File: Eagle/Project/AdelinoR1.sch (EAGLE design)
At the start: 63 parts, among them J1 DC-044-A, J2 YELLOW-8P-2.54, J3 YELLOW-6P-2.54, J4 YELLOW-8P-2.54, J5 YELLOW-8P-2.54, J6 4P-2.0, J7 YELLOW-2X3P-2.54, J8 4P-2.0, Q1 NCE3407A, Q2 CJ2305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

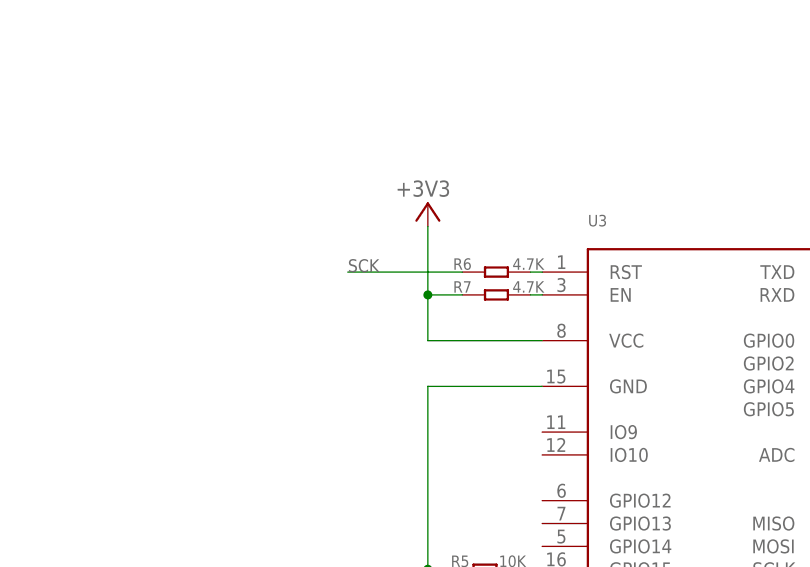
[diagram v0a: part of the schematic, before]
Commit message: Now SCK drives CHIP_EN instead of RST; RST pulled high using 4K7.
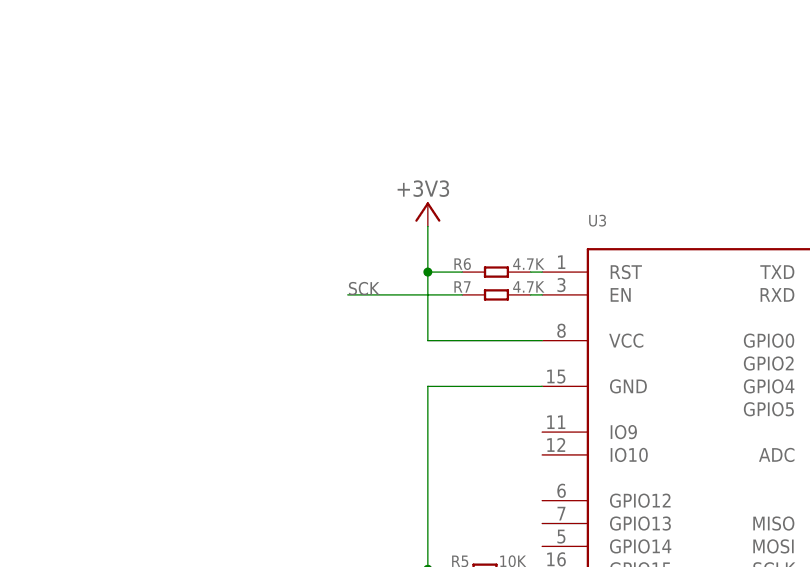
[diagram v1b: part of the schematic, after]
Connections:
- net +3V3: now also R6.1; no longer R7.1
- net SCK: now also R7.1; no longer R6.1
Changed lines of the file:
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@@
 <setting verticaltext="up"/>
 </settings>
-<grid distance="0.1" unitdist="inch" unit="inch" style="lines" multiple="1" display="no" altdistance="0.01" altunitdist="inch" altunit="inch"/>
+<grid distance="0.05" unitdist="inch" unit="inch" style="lines" multiple="1" display="no" altdistance="0.01" altunitdist="inch" altunit="inch"/>
 <layers>
 <layer number="1" name="Top" color="4" fill="1" visible="no" active="no"/>
@@
 <pinref part="+3V32" gate="G$1" pin="+3V3"/>
 <wire x1="93.98" y1="-78.74" x2="81.28" y2="-78.74" width="0.1524" layer="91"/>
-<wire x1="81.28" y1="-78.74" x2="81.28" y2="-73.66" width="0.1524" layer="91"/>
-<wire x1="81.28" y1="-73.66" x2="81.28" y2="-66.04" width="0.1524" layer="91"/>
-<wire x1="85.09" y1="-73.66" x2="81.28" y2="-73.66" width="0.1524" layer="91"/>
-<junction x="81.28" y="-73.66"/>
-<pinref part="R7" gate="G$1" pin="1"/>
+<wire x1="81.28" y1="-78.74" x2="81.28" y2="-71.12" width="0.1524" layer="91"/>
+<pinref part="R6" gate="G$1" pin="1"/>
+<wire x1="81.28" y1="-71.12" x2="81.28" y2="-66.04" width="0.1524" layer="91"/>
+<wire x1="85.09" y1="-71.12" x2="81.28" y2="-71.12" width="0.1524" layer="91"/>
+<junction x="81.28" y="-71.12"/>
 </segment>
 <segment>
@@
 </segment>
 <segment>
-<pinref part="R6" gate="G$1" pin="1"/>
-<wire x1="85.09" y1="-71.12" x2="72.39" y2="-71.12" width="0.1524" layer="91"/>
-<label x="72.39" y="-71.12" size="1.4224" layer="95"/>
-</segment>
-</net>
+<pinref part="R7" gate="G$1" pin="1"/>
+<wire x1="85.09" y1="-73.66" x2="72.39" y2="-73.66" width="0.1524" layer="91"/>
+<label x="72.39" y="-73.66" size="1.4224" layer="95"/>
+</segment>
+</net>

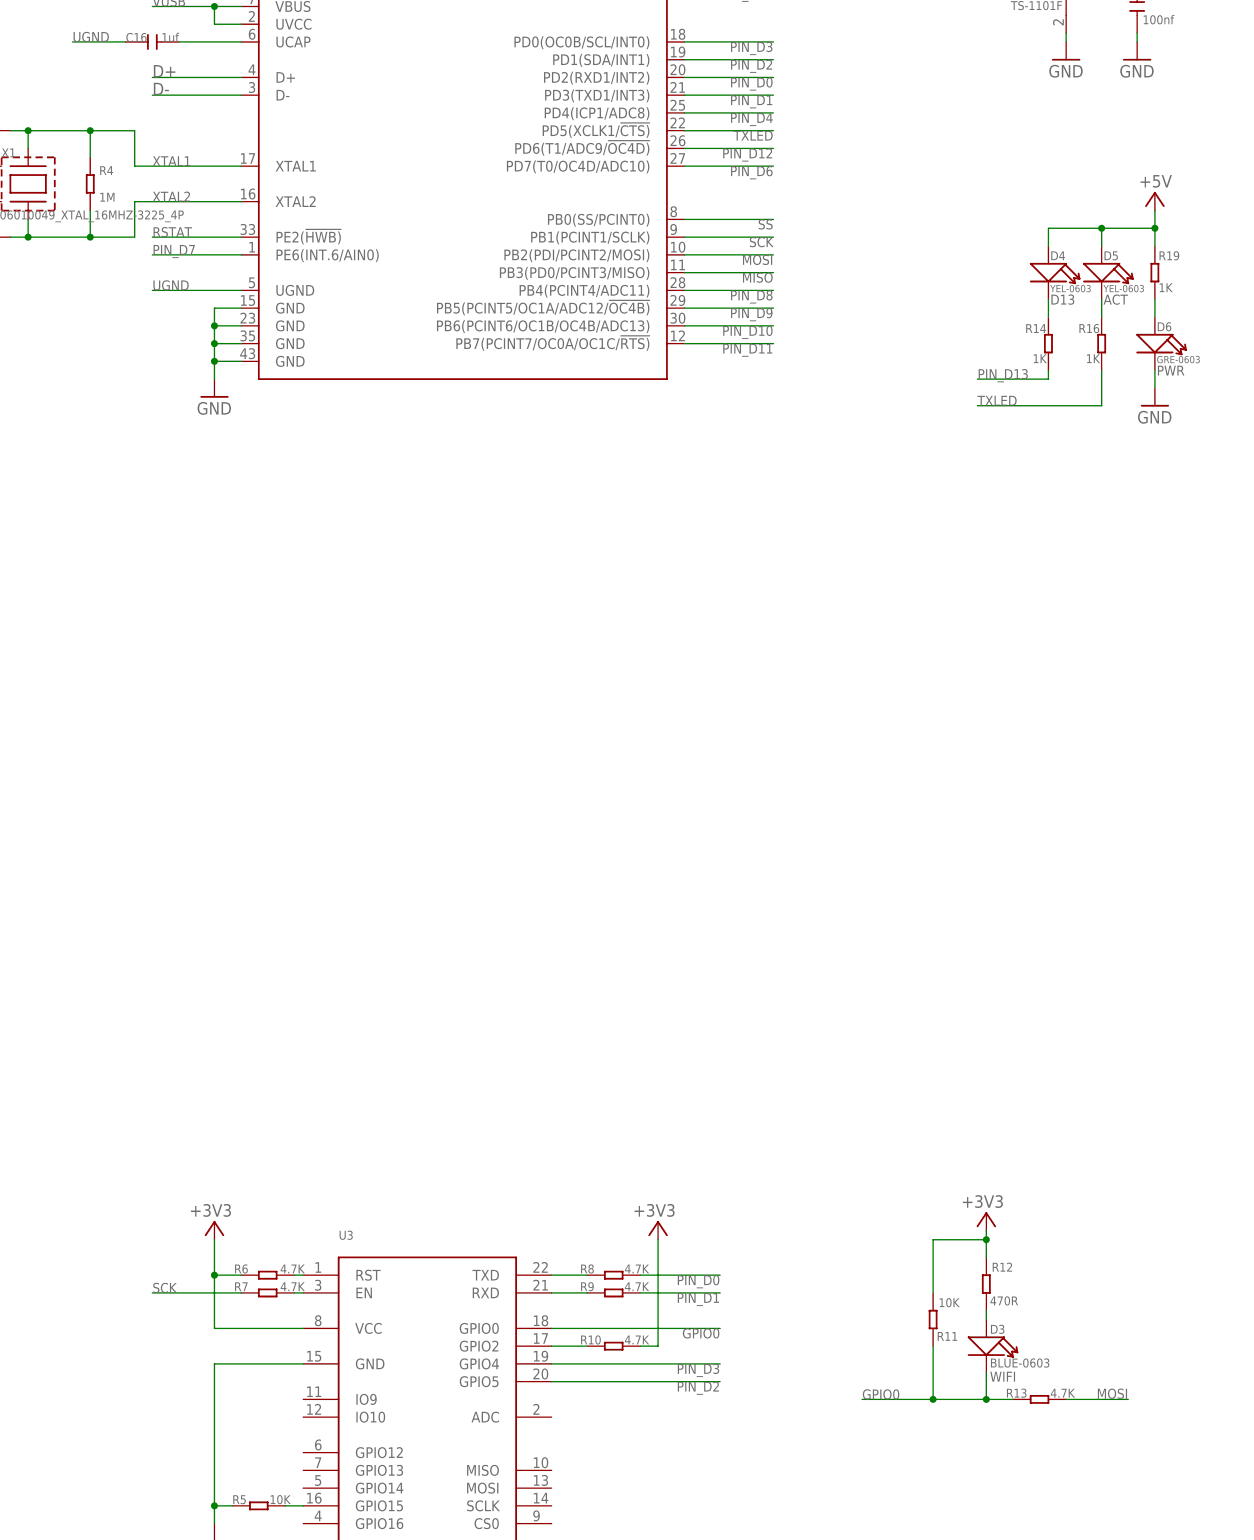
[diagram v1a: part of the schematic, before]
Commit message: Change ACT_LED to PB0; change ESP_EN to PD5; change WIFI led to GPIO2.
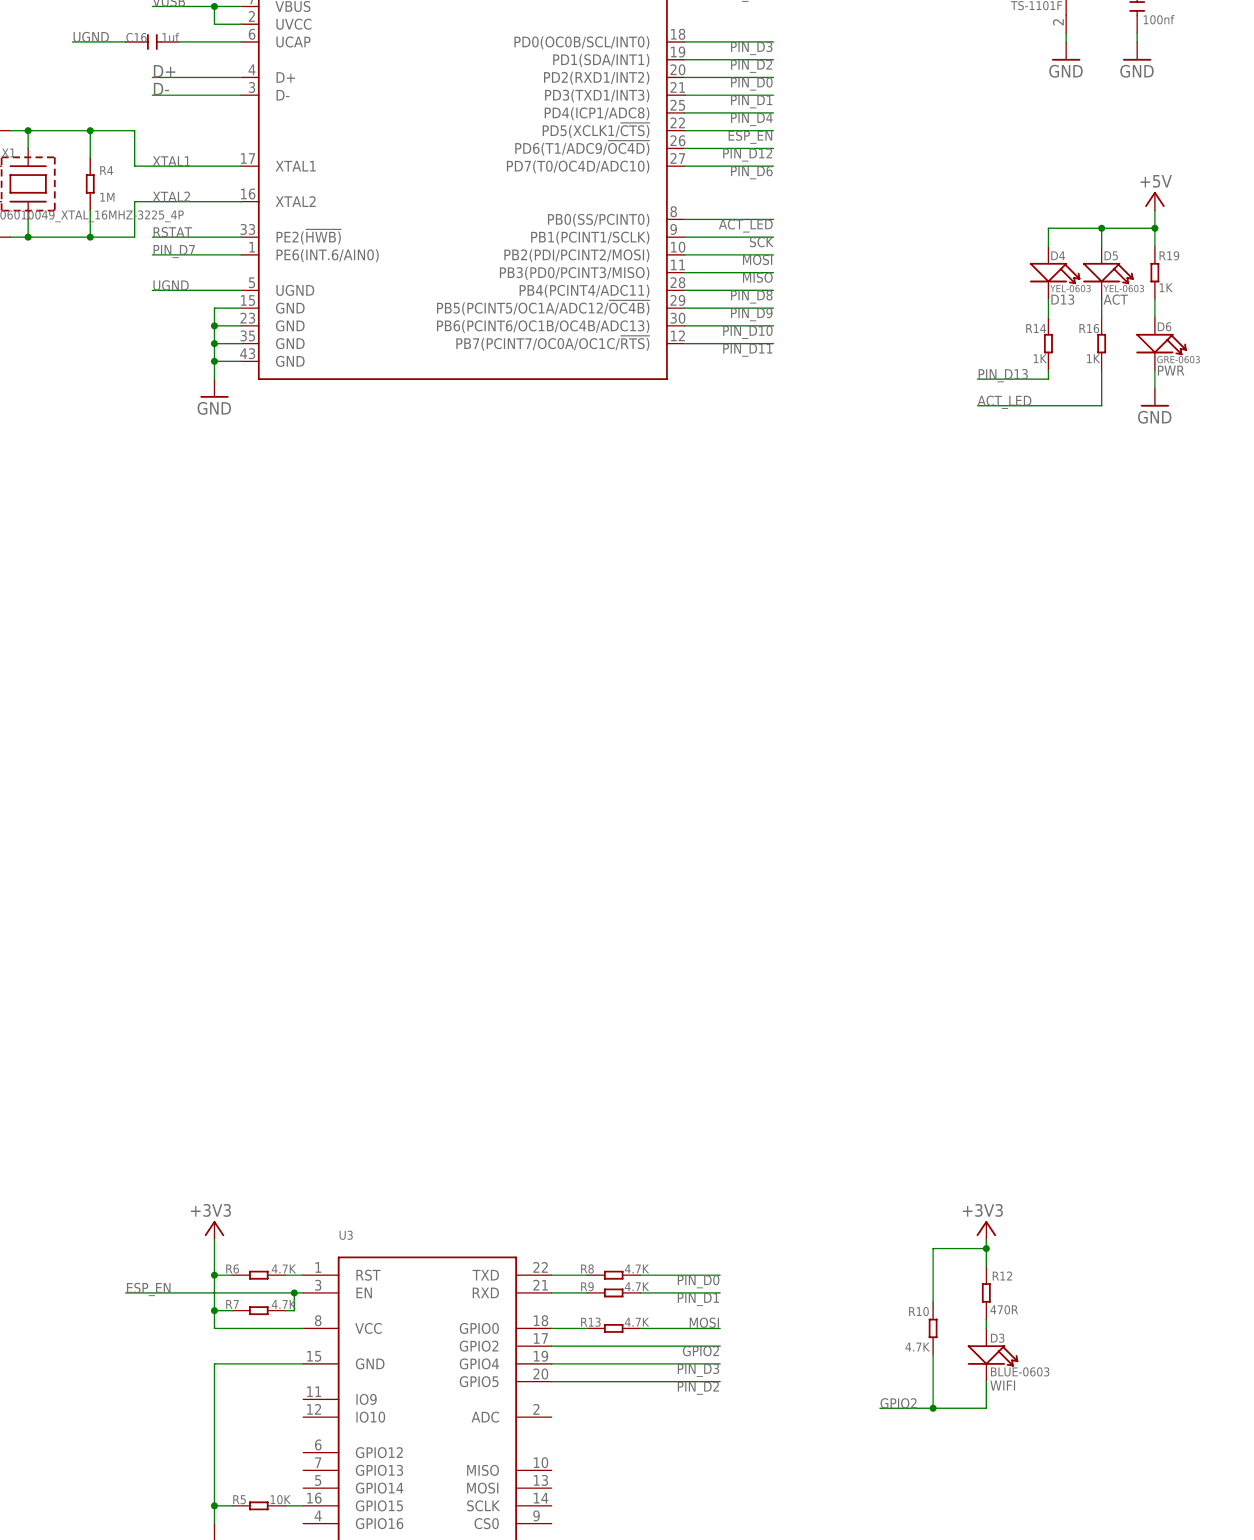
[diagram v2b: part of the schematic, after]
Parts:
- removed R11: 10K, Seeed-Resistor:SMD-RES-10K-1%-1/16W(0402)
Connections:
- removed net N$11: R10.1, U3.GPIO2
- removed net SS: U4.PB0(SS/PCINT0)
- removed net TXLED: R16.2, U4.PD5(XCLK1/!CTS)
- new net ACT_LED: R16.2, U4.PB0(SS/PCINT0)
- new net GPIO2: D3.-, R10.1, U3.GPIO2
- net +3V3: now also R7.1; no longer R11.2
- net ESP_EN: now also U4.PD5(XCLK1/!CTS)
- net GPIO0: no longer D3.-, R11.1
- net SCK: no longer R7.1
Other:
- moved on the sheet: D3, R10, R12, R13, R6, R7

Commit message: Adelino X1 final design.
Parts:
- added R11: 47K, Seeed-Resistor:SMD-RES-47K-5%-1/16W(0402)
- added R20, R21: 1K, Seeed-Resistor:SMD-RES-1K-5%-1/16W(0402)
- added U$1, U$2: MMBT3904LT1G, Seeed-Transistor:SMD-TRANSISTORS-NPN-40V-200MA-MMBT3904LT1G(SOT-23)
- R10, R6, R7: value 4.7K -> 10K 1/16W; device Seeed-Resistor:SMD-RES-4.7K-5%-1/16W(0402) -> Seeed-Resistor:SMD-RES-10K-1%-1/16W(0402)
- R13, R8, R9: value 4.7K -> 1K; device Seeed-Resistor:SMD-RES-4.7K-5%-1/16W(0402) -> Seeed-Resistor:SMD-RES-1K-5%-1/16W(0402)
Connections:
- new net N$16: R20.2, U$1.B
- new net N$21: R21.2, U$2.B
- new net STANDBY1: U$1.C
- new net STANDBY2: U$2.C
- net +3V3: now also R11.2
- net GND: now also U$1.E, U$2.E
- net GPIO0: now also R11.1
- net PIN_D13: now also R21.1
- net PIN_D5: now also R20.1
- net RESET: now also U3.GPIO16
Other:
- moved on the sheet: D3, R10, R12

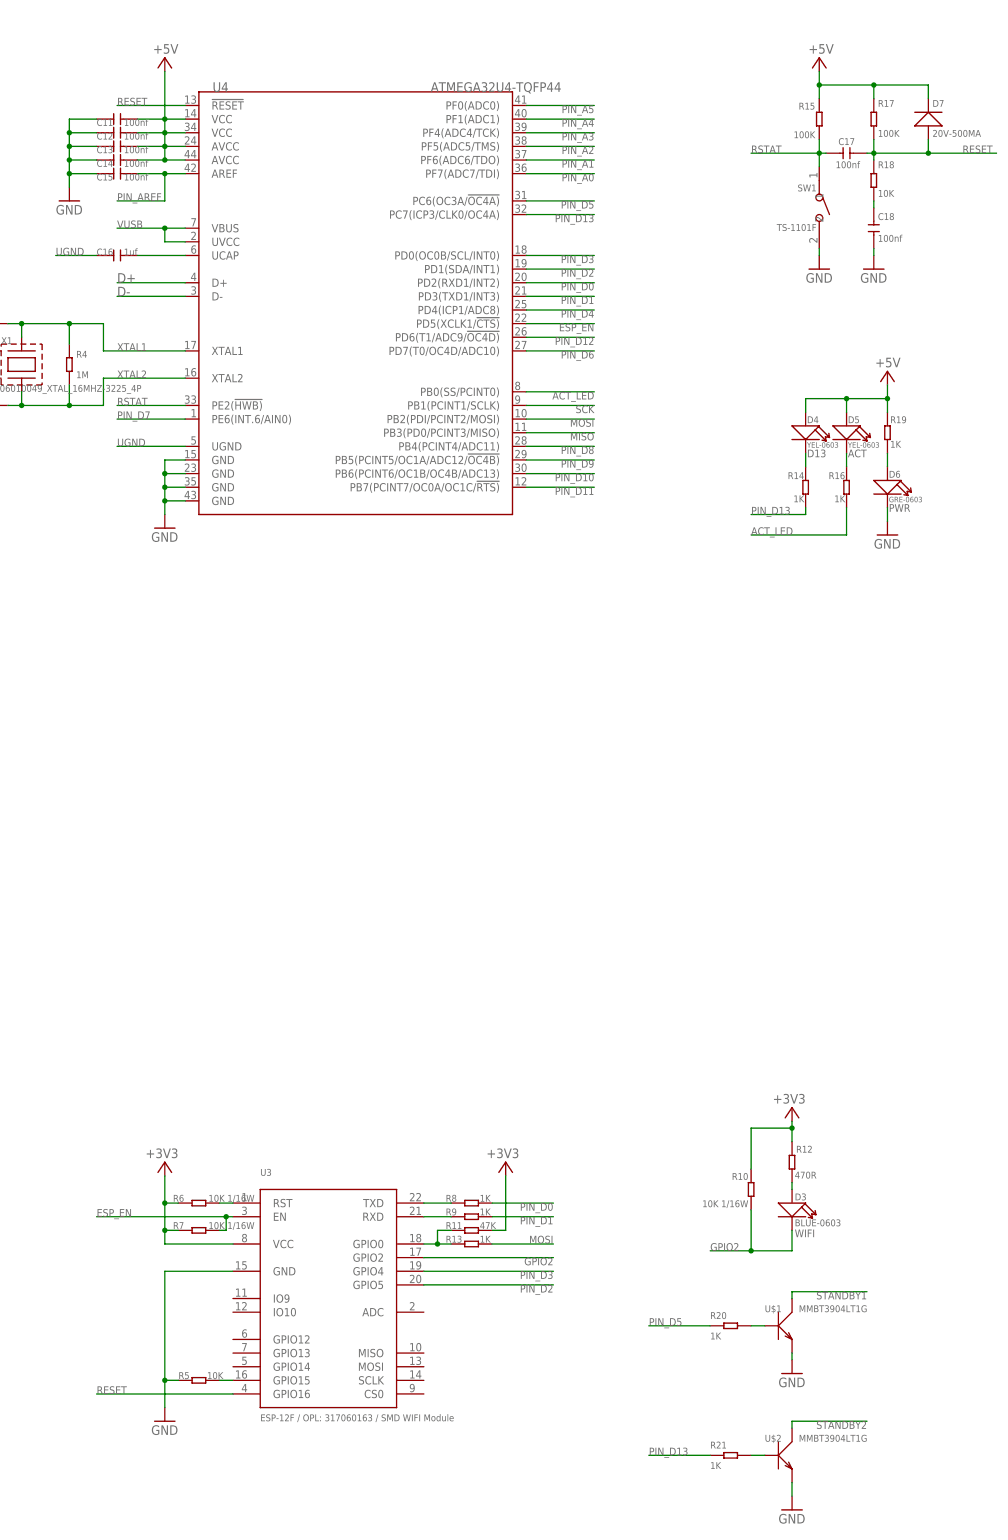
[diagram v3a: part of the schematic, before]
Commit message: Add spare vias for SPI.
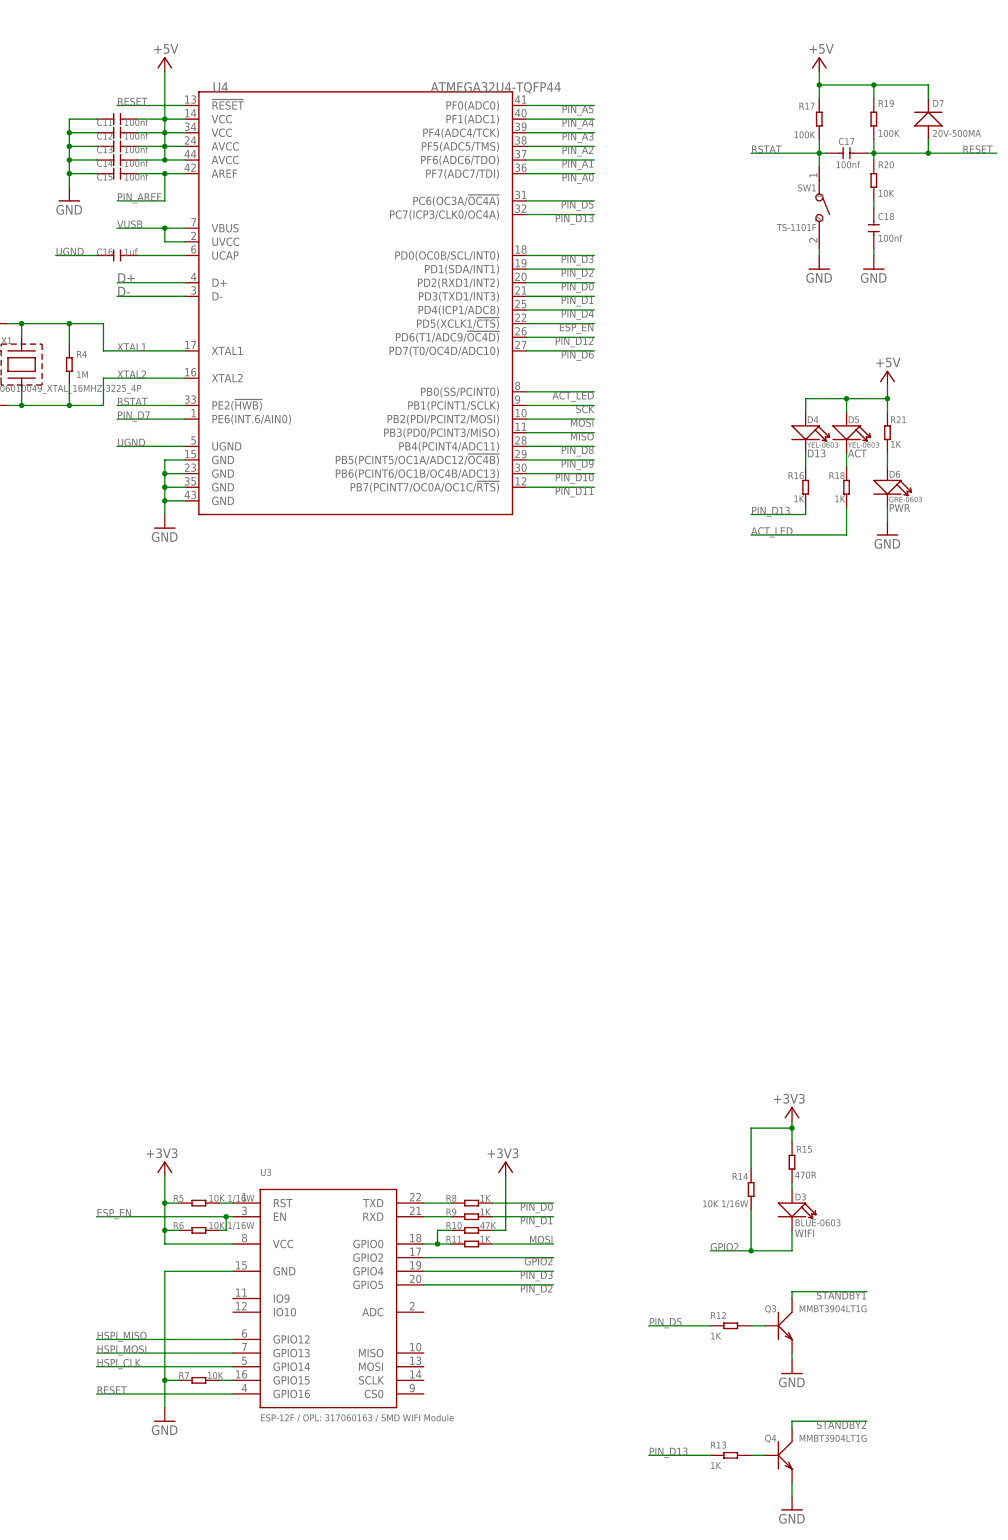
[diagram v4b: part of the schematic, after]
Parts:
- R10: value 10K 1/16W -> 47K; device Seeed-Resistor:SMD-RES-10K-1%-1/16W(0402) -> Seeed-Resistor:SMD-RES-47K-5%-1/16W(0402)
- R11: value 47K -> 1K; device Seeed-Resistor:SMD-RES-47K-5%-1/16W(0402) -> Seeed-Resistor:SMD-RES-1K-5%-1/16W(0402)
- R12: value 470R -> 1K; device Seeed-Resistor:SMD-RES-470R-5%-1/16W(0402) -> Seeed-Resistor:SMD-RES-1K-5%-1/16W(0402)
- R14: value 1K -> 10K 1/16W; device Seeed-Resistor:SMD-RES-1K-5%-1/16W(0402) -> Seeed-Resistor:SMD-RES-10K-1%-1/16W(0402)
- R15: value 100K -> 470R; device Seeed-Resistor:SMD-RES-100K-1%-1/16W(0402) -> Seeed-Resistor:SMD-RES-470R-5%-1/16W(0402)
- R18: value 10K -> 1K; device Seeed-Resistor:SMD-RES-10K-1%-1/16W(0402) -> Seeed-Resistor:SMD-RES-1K-5%-1/16W(0402)
- R19: value 1K -> 100K; device Seeed-Resistor:SMD-RES-1K-5%-1/16W(0402) -> Seeed-Resistor:SMD-RES-100K-1%-1/16W(0402)
- R20: value 1K -> 10K; device Seeed-Resistor:SMD-RES-1K-5%-1/16W(0402) -> Seeed-Resistor:SMD-RES-10K-1%-1/16W(0402)
- R5: value 10K -> 10K 1/16W
- R7: value 10K 1/16W -> 10K
- renumbered U$1 to Q3, U$2 to Q4
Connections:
- new net HSPI_CLK: U3.GPIO14
- new net HSPI_MISO: U3.GPIO12
- new net HSPI_MOSI: U3.GPIO13
- net +3V3: now also R14.2, R15.2, R5.1; no longer R11.2, R12.2, R7.1
- net +5V: now also R17.1, R19.2, R21.1; no longer R15.1, R17.2, R19.1
- net ACT_LED: now also R18.2; no longer R16.2
- net ESP_EN: now also R6.2; no longer R7.2
- net GND: now also R7.1; no longer R5.1
- net GPIO0: now also R10.1; no longer R13.1
- net GPIO2: now also R14.1; no longer R10.1
- net MOSI: now also R11.2; no longer R13.2
- net N$12: now also R15.1; no longer R12.1
- net N$13: now also R20.2; no longer R18.2
- net N$14: now also R5.2; no longer R6.2
- net N$16: now also R12.2; no longer R20.2
- net N$21: now also R13.2; no longer R21.2
- net N$4: now also R7.2; no longer R5.2
- net N$5: now also R21.2; no longer R19.2
- net N$6: now also R18.1; no longer R16.1
- net N$8: now also R16.1; no longer R14.1
- net PIN_D13: now also R13.1, R16.2; no longer R14.2, R21.1
- net PIN_D5: now also R12.1; no longer R20.1
- net RESET: now also R19.1, R20.1; no longer R17.1, R18.1
- net RSTAT: now also R17.2; no longer R15.2
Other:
- moved on the sheet: R10, R11, R12, R13, R14, R15, R16, R17, R18, R19, R20, R21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
